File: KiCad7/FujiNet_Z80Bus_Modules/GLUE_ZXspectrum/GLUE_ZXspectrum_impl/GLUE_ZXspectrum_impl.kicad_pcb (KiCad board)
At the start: 2 copper layers, 0 parts

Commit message: KiCad FIXED GLUE
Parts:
- added C1: 10UF, Capacitor_THT:CP_Radial_D8.0mm_P5.00mm, F.Cu at (122.0, 136.6)
- added C2: 10UF, Capacitor_THT:CP_Radial_D8.0mm_P5.00mm, F.Cu at (157.0, 131.6)
- added D1: 1N4148, Diode_THT:D_T-1_P5.08mm_Horizontal, F.Cu at (140.0, 104.0)
- added D2: 1N4148, Diode_THT:D_T-1_P5.08mm_Horizontal, F.Cu at (172.3, 136.0)
- added D3: 1N4148, Diode_THT:D_T-1_P5.08mm_Horizontal, F.Cu at (174.0, 88.1)
- added D4: 1N4148, Diode_THT:D_T-1_P5.08mm_Horizontal, F.Cu at (187.1, 91.0)
- added IC1: 7404N, Package_DIP:DIP-14_W7.62mm_Socket, F.Cu at (149.0, 112.0)
- added IC2: 74HC32N, Package_DIP:DIP-14_W7.62mm_Socket, F.Cu at (123.5, 76.0)
- added IC3: 7474N, Package_DIP:DIP-14_W7.62mm_Socket, F.Cu at (119.4, 111.8)
- added IC4: 74HC08N, Package_DIP:DIP-14_W7.62mm_Socket, F.Cu at (134.0, 136.6)
- added IC5: 74HC32N, Package_DIP:DIP-14_W7.62mm_Socket, F.Cu at (148.9, 75.6)
- added IC6: 74HC08N, Package_DIP:DIP-14_W7.62mm_Socket, F.Cu at (149.0, 94.0)
- added IC7: 74HC32N, Package_DIP:DIP-14_W7.62mm_Socket, F.Cu at (173.5, 111.5)
- added IC8: 74HC08N, Package_DIP:DIP-14_W7.62mm_Socket, F.Cu at (123.5, 94.0)
- added IC9: 74HC32N, Package_DIP:DIP-14_W7.62mm_Socket, F.Cu at (174.4, 75.8)
- added J1: Conn_01x24_Socket, Connector_PinSocket_2.54mm:PinSocket_1x24_P2.54mm_Vertical, F.Cu at (202.0, 68.0)
- added J2: Conn_01x26_Socket, Connector_PinSocket_2.54mm:PinSocket_1x26_P2.54mm_Vertical, F.Cu at (110.0, 68.0)
- added R1: 22K, Resistor_THT:R_Axial_DIN0207_L6.3mm_D2.5mm_P10.16mm_Horizontal, F.Cu at (129.0, 126.4)
- added R2: 22K, Resistor_THT:R_Axial_DIN0207_L6.3mm_D2.5mm_P10.16mm_Horizontal, F.Cu at (134.0, 123.6)
- added R3: 10K, Resistor_THT:R_Axial_DIN0207_L6.3mm_D2.5mm_P10.16mm_Horizontal, F.Cu at (178.8, 83.0)
- added R4: 10K, Resistor_THT:R_Axial_DIN0207_L6.3mm_D2.5mm_P10.16mm_Horizontal, F.Cu at (172.0, 95.9)
- added RN1: 4609M-101-103LF, Resistor_THT:R_Array_SIP9, F.Cu at (176.7, 136.0)
- added U1: 74HC244N, Package_DIP:DIP-20_W7.62mm_Socket, F.Cu at (168.5, 127.6)
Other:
- board outline added: 100 x 89 mm

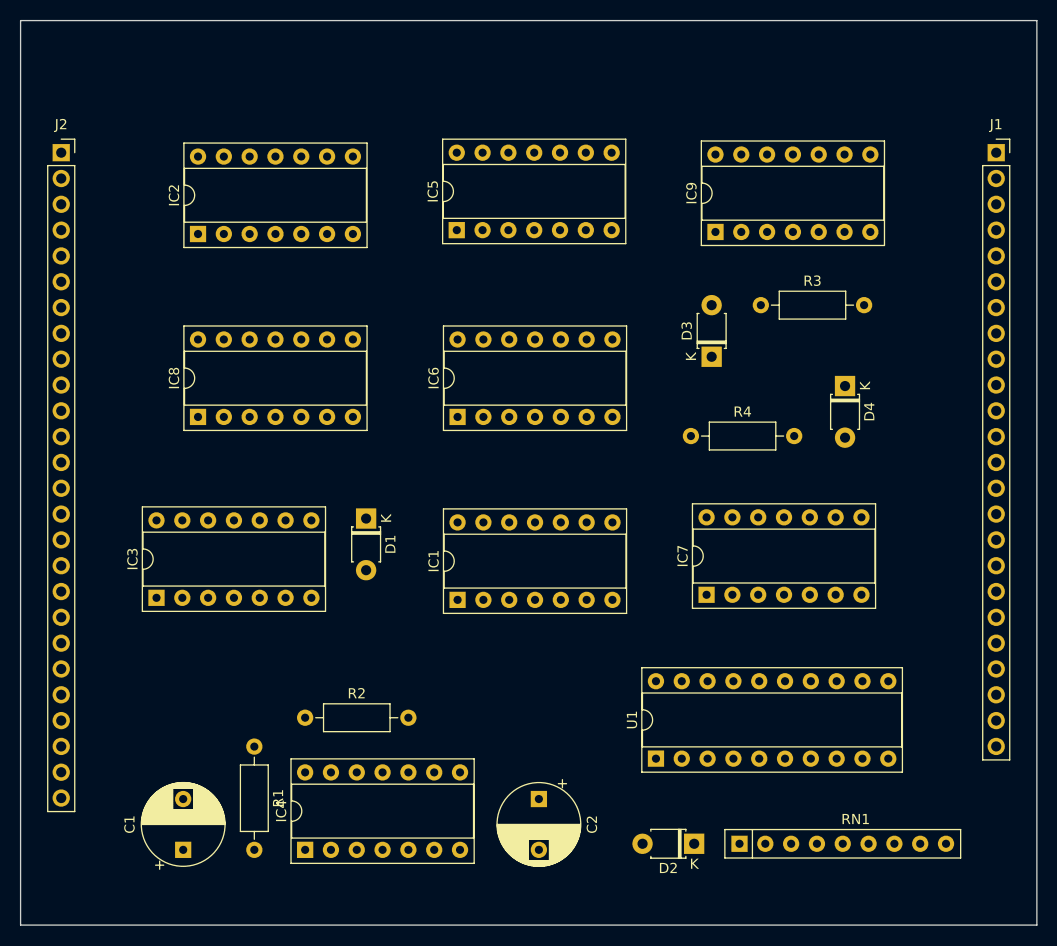
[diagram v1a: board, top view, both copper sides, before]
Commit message: KiCad GLUE PCB routed
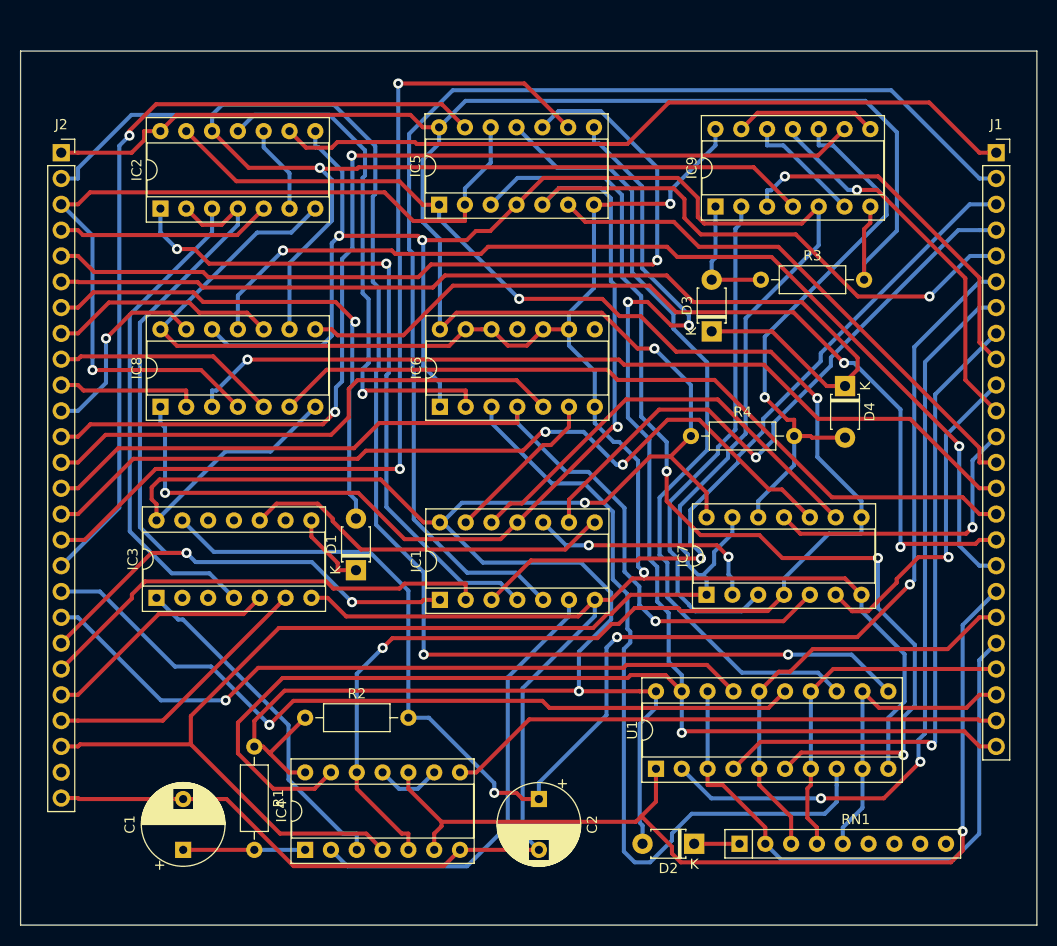
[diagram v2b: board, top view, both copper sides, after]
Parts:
- moved D1 5.18 mm to (139.0, 109.1), turned to 90 degrees
- moved IC2 4.47 mm to (119.8, 73.5)
- moved IC8 3.83 mm to (119.8, 93.0)
- moved IC5 3.05 mm to (147.2, 73.1)
- moved D3 2.50 mm to (174.0, 85.6)
- moved IC9 2.50 mm to (174.4, 73.3)
- moved R3 2.50 mm to (178.8, 80.5)
- moved IC6 2.01 mm to (147.3, 93.0)
- moved IC1 1.74 mm to (147.3, 112.0)
- moved U1 1.00 mm to (168.5, 128.6)
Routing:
- net +5V: track 0.00 -> 355.4 mm, vias 0 -> 3
- net GND: track 0.00 -> 276.2 mm, vias 0 -> 2
- net /PERM_Z80_IORQ: track 0.00 -> 251.9 mm, vias 0 -> 2
- net /Z80_CONTROL.RD: track 0.00 -> 215.9 mm, vias 0 -> 3
- net /RIO_CONTROL.ROM_RDY: track 0.00 -> 167.4 mm, vias 0 -> 3
- net /GLUE_ZXspectrum/ESP_IOD_CONFIG: track 0.00 -> 165.4 mm, vias 0 -> 3
- net /CACHE_DATASTATUS: track 0.00 -> 142.8 mm, vias 0 -> 3
- net /ESP_WAIT_RESET: track 0.00 -> 138.7 mm, vias 0 -> 3
- net /Z80_HARDLOCK_RESET: track 0.00 -> 117.3 mm
- net /GLUE_ZXspectrum/RIO CONTROL/Z80_WR+ESP_IOD_CONFIG: track 0.00 -> 103.5 mm, vias 0 -> 3
- net /ESP_CONTROL.WR: track 0.00 -> 103.5 mm, vias 0 -> 2
- net /Z80_CONTROL.BUSRQ: track 0.00 -> 101.3 mm
- net /CACHE_CONTROL.CS: track 0.00 -> 99.0 mm, vias 0 -> 2
- net /RIO_CONTROL.A16: track 0.00 -> 95.6 mm, vias 0 -> 1
- net /ESP_CONTROL.MEMRQ: track 0.00 -> 93.4 mm, vias 0 -> 1
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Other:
- board size 100 x 89 mm -> 100 x 86 mm
